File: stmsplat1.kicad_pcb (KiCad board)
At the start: 2 copper layers, 72 parts, among them CN1 Conn_01x16_Male, CN2 Conn_01x30_Male, CN3 Conn_01x20_Male, CN4 Conn_01x34_Male, J1 Conn_Coaxial, J2 Conn_01x04_Male, J3 Conn_01x04_Male, U1 NUCLEO144-F746ZG, U10 MPL315A2, U11 XBee3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

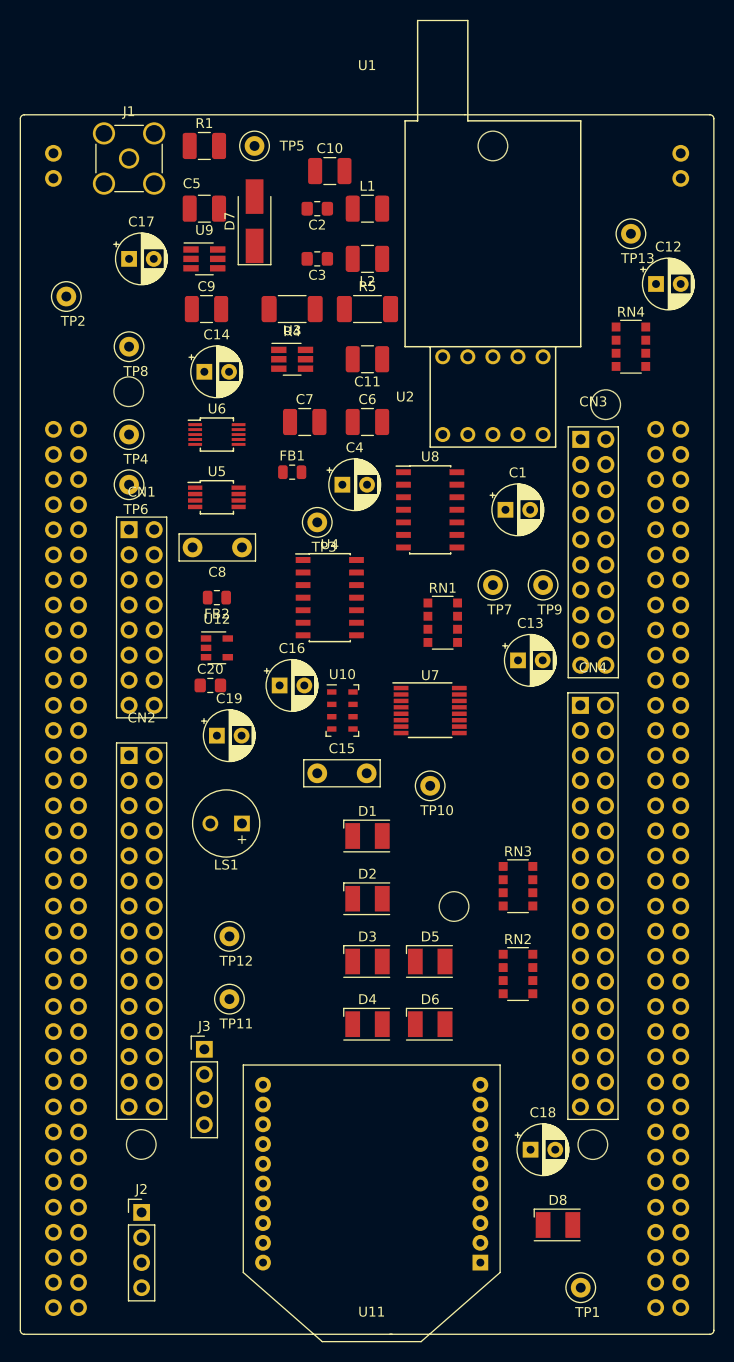
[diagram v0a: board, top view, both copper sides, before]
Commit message: silkscreen mods, small placement changes
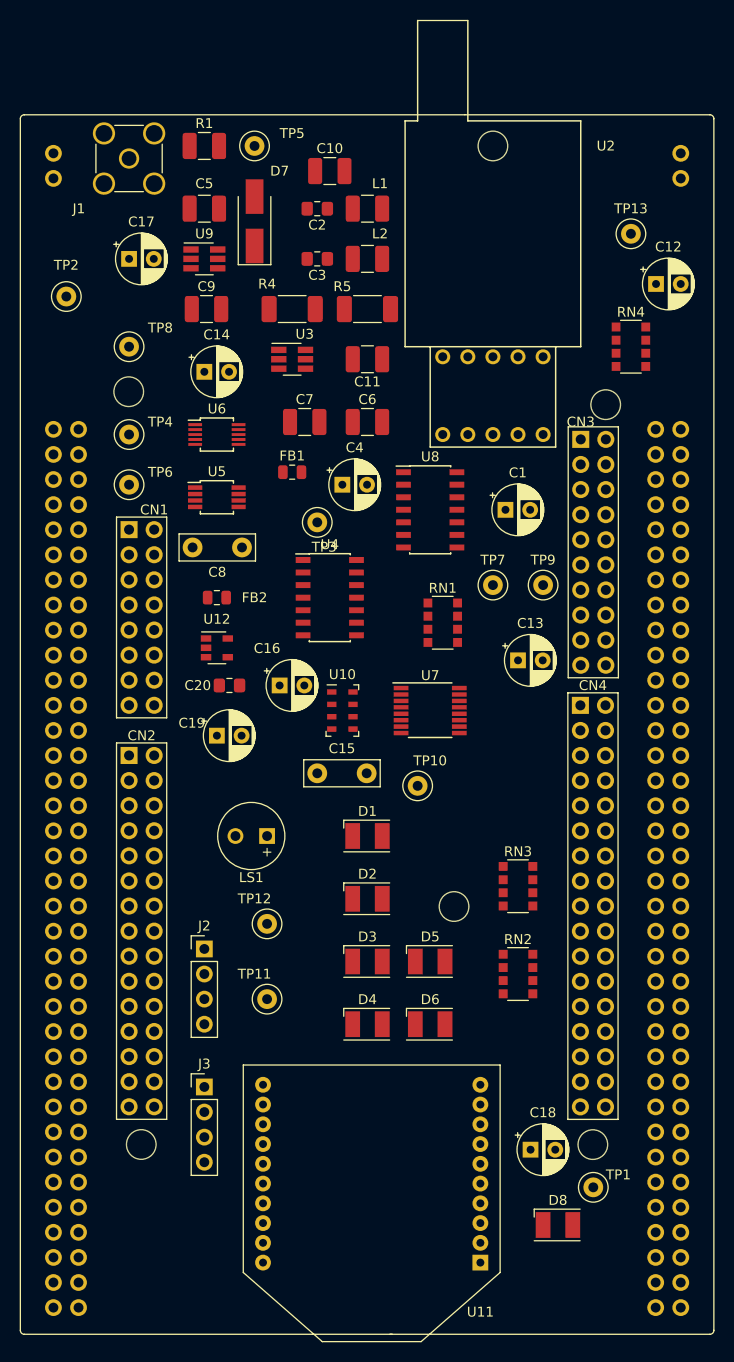
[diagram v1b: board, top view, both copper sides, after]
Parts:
- moved J2 27.4 mm to (73.7, 118.1)
- moved TP1 10.2 mm to (113.0, 142.2)
- moved TP12 4.02 mm to (80.0, 115.6)
- moved J3 3.81 mm to (73.7, 132.1)
- moved TP11 3.81 mm to (80.0, 123.2)
- moved LS1 2.84 mm to (80.0, 106.7)
- moved C20 1.93 mm to (76.2, 91.4), turned to 180 degrees
- moved TP10 1.27 mm to (95.2, 101.6)
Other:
- net class Default: clearance 0.2 -> 0.25
- rule trace_clearance: 0.2 -> 0.25
- rule trace_min: 0.2 -> 0.25

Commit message: 2nd go at manual routing. Via sizes may all be small.
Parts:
- added C21: 100uF, Capacitor_THT:CP_Radial_D5.0mm_P2.50mm, F.Cu at (66.0, 70.5)
- moved TP6 14.7 mm to (64.1, 56.5)
- moved TP4 9.86 mm to (68.6, 56.5)
- moved TP8 6.38 mm to (59.7, 56.5)
- moved TP2 3.17 mm to (59.7, 48.9)
- moved FB2 2.01 mm to (74.3, 80.6)
- moved C17 1.91 mm to (64.1, 48.3)
- turned D8 to 180 degrees
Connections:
- J2 pad 1: /5V0 -> /+5V
- J3 pad 1: /5V0 -> /+5V
- U11 pad 5: /PE15 -> Net-(D8-Pad2)
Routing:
- net GND: track 0.00 -> 466.0 mm, vias 0 -> 3
- net AGND: track 0.00 -> 232.4 mm, vias 0 -> 6
- net /P3V3: track 0.00 -> 212.9 mm, vias 0 -> 4
- net /A3V3: track 0.00 -> 122.5 mm, vias 0 -> 5
- net /+5V: track 0.00 -> 114.9 mm, vias 0 -> 3
- net /PB15: track 0.00 -> 100.2 mm, vias 0 -> 2
- net /PB12: track 0.00 -> 96.2 mm, vias 0 -> 1
- net /PB10: track 0.00 -> 95.8 mm, vias 0 -> 2
- net /PC11: track 0.00 -> 94.3 mm, vias 0 -> 1
- net /PA15: track 0.00 -> 86.2 mm, vias 0 -> 2
- net /PA7: track 0.00 -> 84.3 mm, vias 0 -> 4
- net /PE14: track 0.00 -> 78.6 mm, vias 0 -> 2
- net Net-(U11-Pad7): track 0.00 -> 73.0 mm, vias 0 -> 1
- net /PC2: track 0.00 -> 71.9 mm, vias 0 -> 2
- net /LOGOUT: track 0.00 -> 70.1 mm, vias 0 -> 5
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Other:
- net class Default: clearance 0.25 -> 0.2
- rule trace_clearance: 0.25 -> 0.2
- rule trace_min: 0.25 -> 0.2

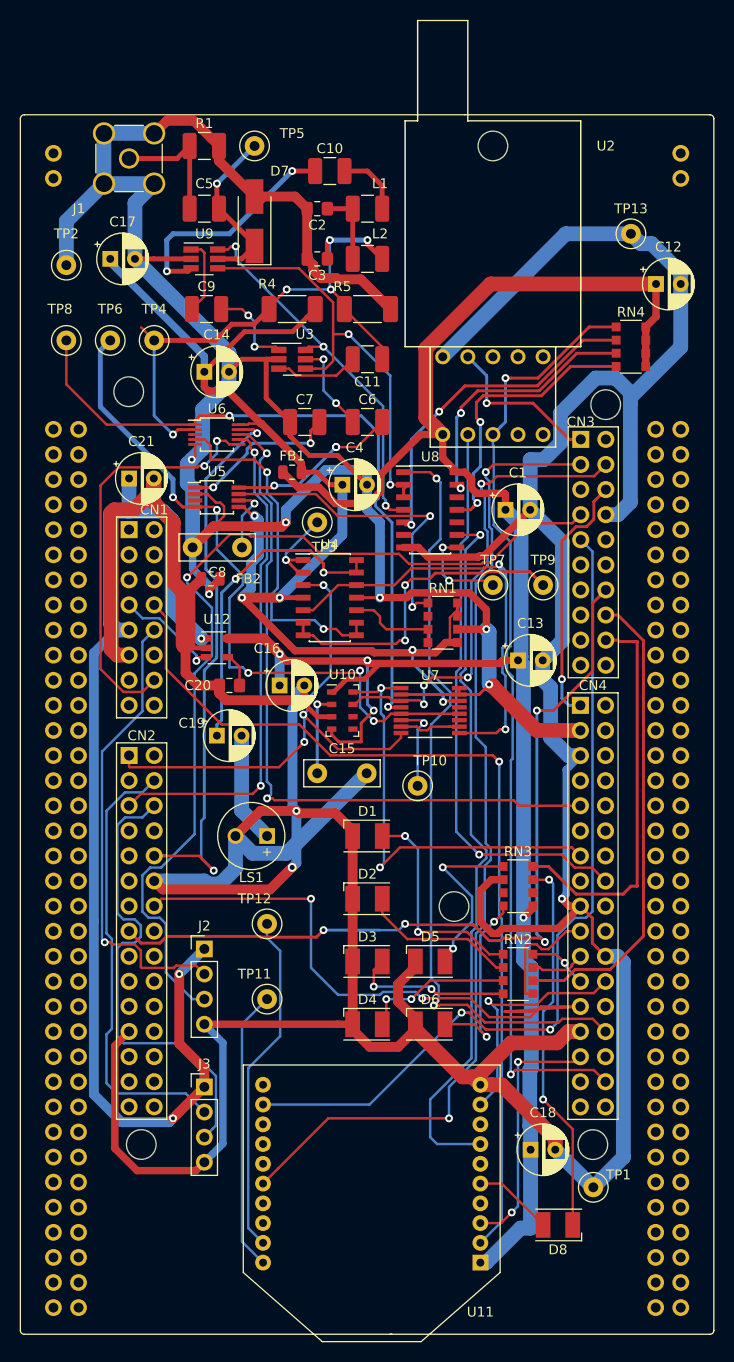
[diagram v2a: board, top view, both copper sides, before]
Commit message: Fix Xbee extra symbol pin, change via sizes on power
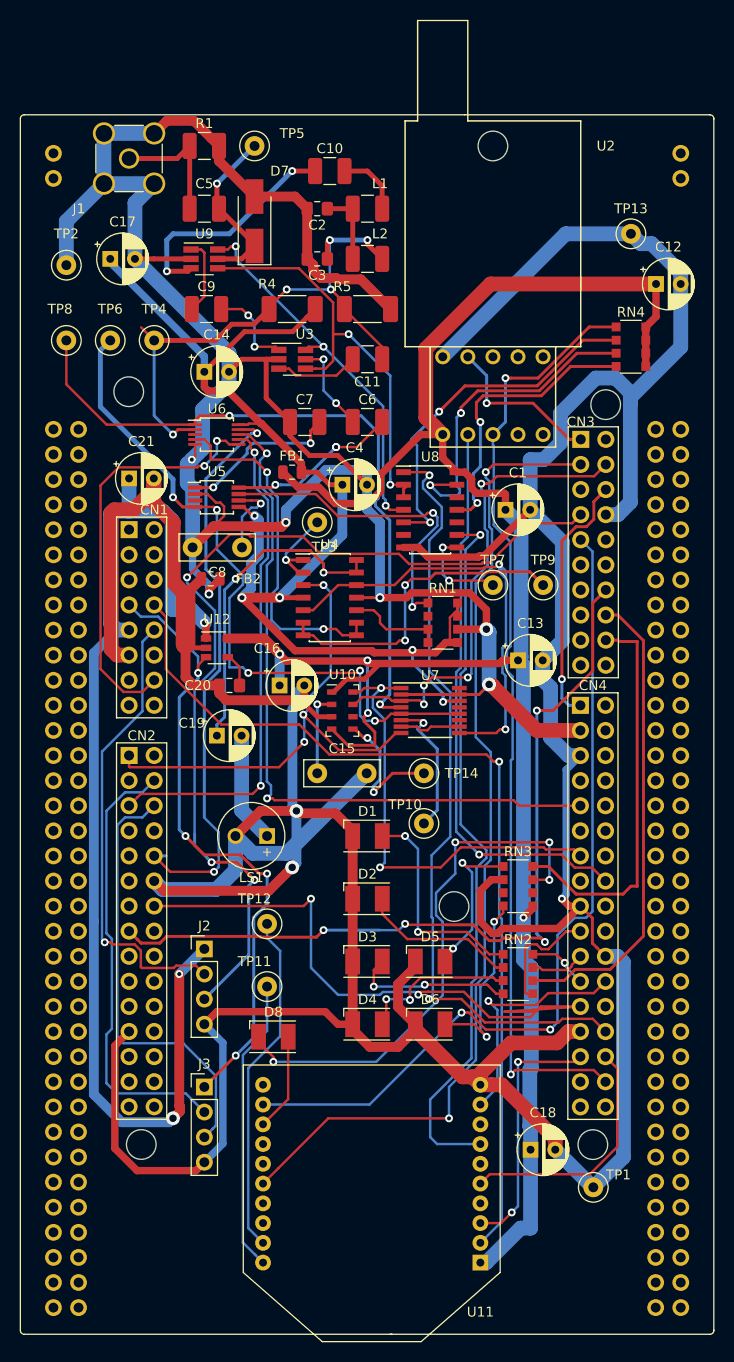
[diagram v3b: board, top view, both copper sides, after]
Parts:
- added TP14: TestPoint, TestPoint:TestPoint_Loop_D1.80mm_Drill1.0mm_Beaded, F.Cu at (95.9, 100.3)
- moved D8 34.5 mm to (80.6, 127.0), turned to 0 degrees
- moved TP10 3.86 mm to (95.9, 105.4)
- moved TP11 1.27 mm to (80.0, 121.9)
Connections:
- J3 pad 1: /+5V -> /+3V3
- U11 pad 13: Net-(U11-Pad13) -> Net-(D8-Pad2)
- U11 pad 5: Net-(D8-Pad2) -> /PE15
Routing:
- net /+3V3: track 10.7 -> 64.3 mm, vias 1 -> 4
- net /PE15: track 0.00 -> 25.0 mm
- net /XB_PIO4: track 38.4 -> 54.7 mm, vias 2 -> 4
- net Net-(TP14-Pad1): track 0.00 -> 14.0 mm, vias 0 -> 2
- net Net-(RN4-Pad3): track 27.0 -> 33.2 mm
- net Net-(TP10-Pad1): track 9.05 -> 14.2 mm
- net /PD5: track 47.6 -> 44.3 mm
- net Net-(RN4-Pad2): track 34.4 -> 36.8 mm
- net Net-(D5-Pad2): track 18.0 -> 15.8 mm
- net GND: track 466.0 -> 467.9 mm
- net Net-(D8-Pad2): track 8.09 -> 9.91 mm
- net /P3V3: track 212.9 -> 214.3 mm
- net /+5V: track 114.9 -> 113.6 mm
- net Net-(RN1-Pad1): track 32.0 -> 33.3 mm
- net Net-(C8-Pad1): track 6.71 -> 7.93 mm
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
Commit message: Before splitting drive to RF switches
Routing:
- net /A3V3: track 122.5 -> 126.3 mm
- net GND: track 467.9 -> 470.4 mm
- net /P3V3: track 214.3 -> 213.7 mm
- added copper zone on F.Cu, net /A3V3
- added copper zone on B.Cu, net AGND
- added copper zone on B.Cu, net GND

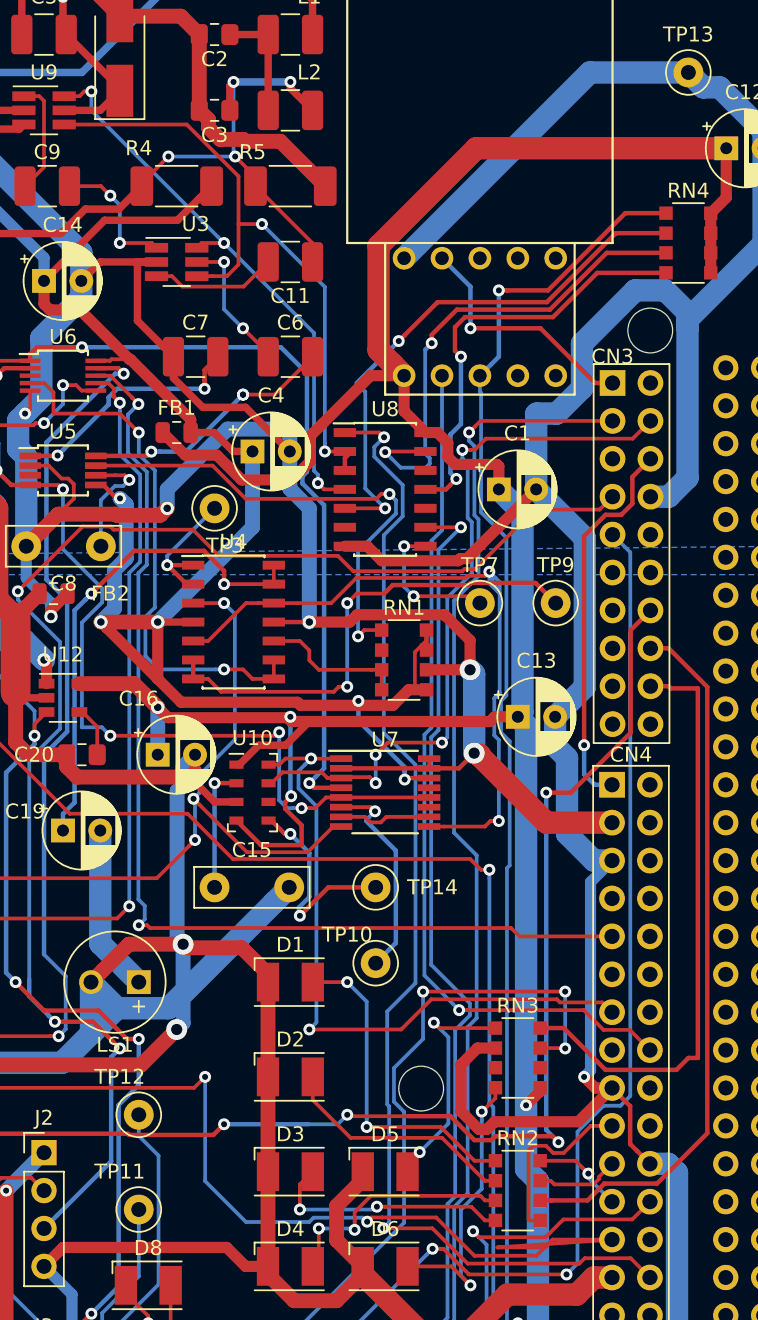
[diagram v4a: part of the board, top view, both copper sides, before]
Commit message: Split drive to RF switches
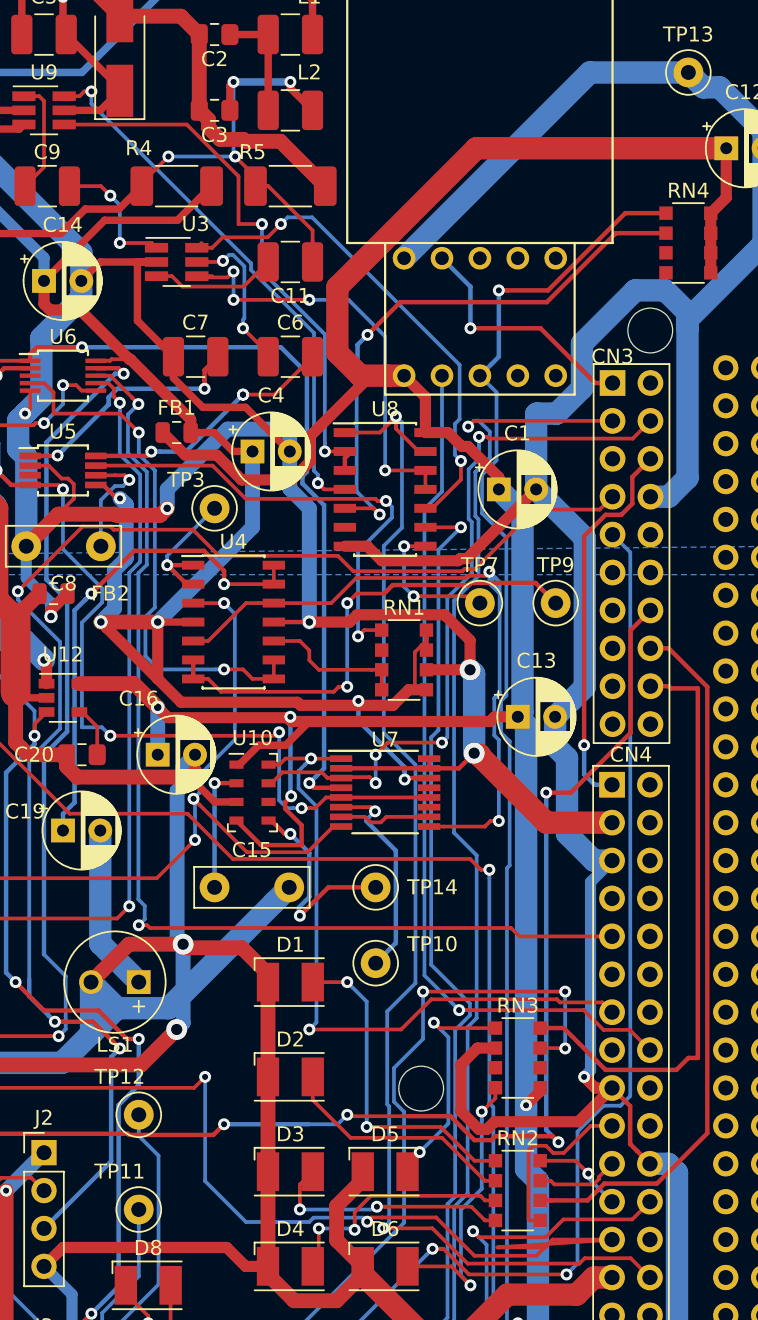
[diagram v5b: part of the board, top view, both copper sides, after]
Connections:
- U8 pad 10: Net-(U8-Pad10) -> Net-(U3-Pad6)
- U8 pad 11: Net-(RN4-Pad4) -> Net-(U3-Pad4)
- U8 pad 12: Net-(U8-Pad12) -> Net-(U3-Pad4)
- U8 pad 13: Net-(RN4-Pad3) -> /PE14
- U8 pad 2: Net-(U3-Pad4) -> Net-(U8-Pad2)
- U8 pad 3: Net-(U3-Pad4) -> Net-(U8-Pad2)
- U8 pad 4: Net-(U3-Pad6) -> Net-(U8-Pad4)
- U9 pad 4: Net-(U3-Pad4) -> Net-(U8-Pad2)
- U9 pad 6: Net-(U3-Pad6) -> Net-(U8-Pad4)
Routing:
- net Net-(U8-Pad2): track 0.00 -> 38.1 mm, vias 0 -> 2
- net Net-(U8-Pad4): track 0.00 -> 36.5 mm, vias 0 -> 2
- net Net-(RN4-Pad3): track 33.2 -> 0.00 mm, vias 2 -> 0
- net Net-(RN4-Pad4): track 28.8 -> 0.00 mm, vias 2 -> 0
- net Net-(U3-Pad4): track 44.0 -> 29.7 mm, vias 2 -> 4
- net /PE14: track 78.8 -> 83.8 mm
- net Net-(U3-Pad6): track 38.4 -> 34.2 mm, vias 3 -> 2
- net /PB15: track 100.2 -> 102.3 mm
- net /P3V3: track 213.7 -> 215.6 mm
- net Net-(RN4-Pad2): track 36.8 -> 38.3 mm
- net Net-(C6-Pad1): track 9.40 -> 10.5 mm
- net Net-(RN1-Pad1): track 33.3 -> 32.4 mm
- net /PB10: track 95.8 -> 96.6 mm
- net Net-(C11-Pad1): track 57.4 -> 57.9 mm
